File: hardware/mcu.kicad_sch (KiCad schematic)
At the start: 36 parts, among them U1 74LVC125, U2 STM32F407VETx, U3 24LC64, U7 74LVC125, X1 12MHz

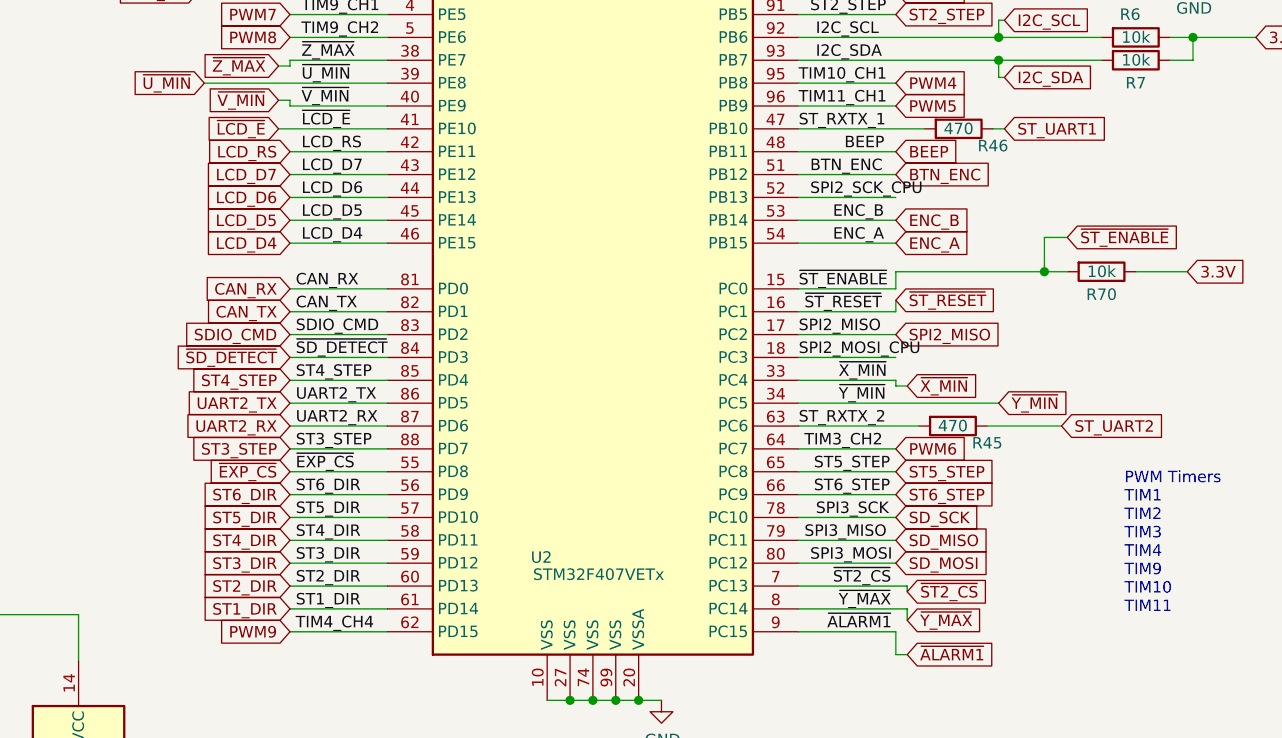
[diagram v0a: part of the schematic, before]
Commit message: Wire sd-card to SPI1, add sd_card_ss (~SD_CS) pin. Add EXP_CD pin for EXP2.4. Add dedicated EXP_SS pin for EXP2.7 - no longer has to share ~SD_DETECT. Added new pin ~EXP_CS2, replaced 3.3V supply on EXP3.
Removed 3.3V power supply from extension header. The 3.3V power supply is
very limited (500mA) and we need it clean for the ADCs to work well.
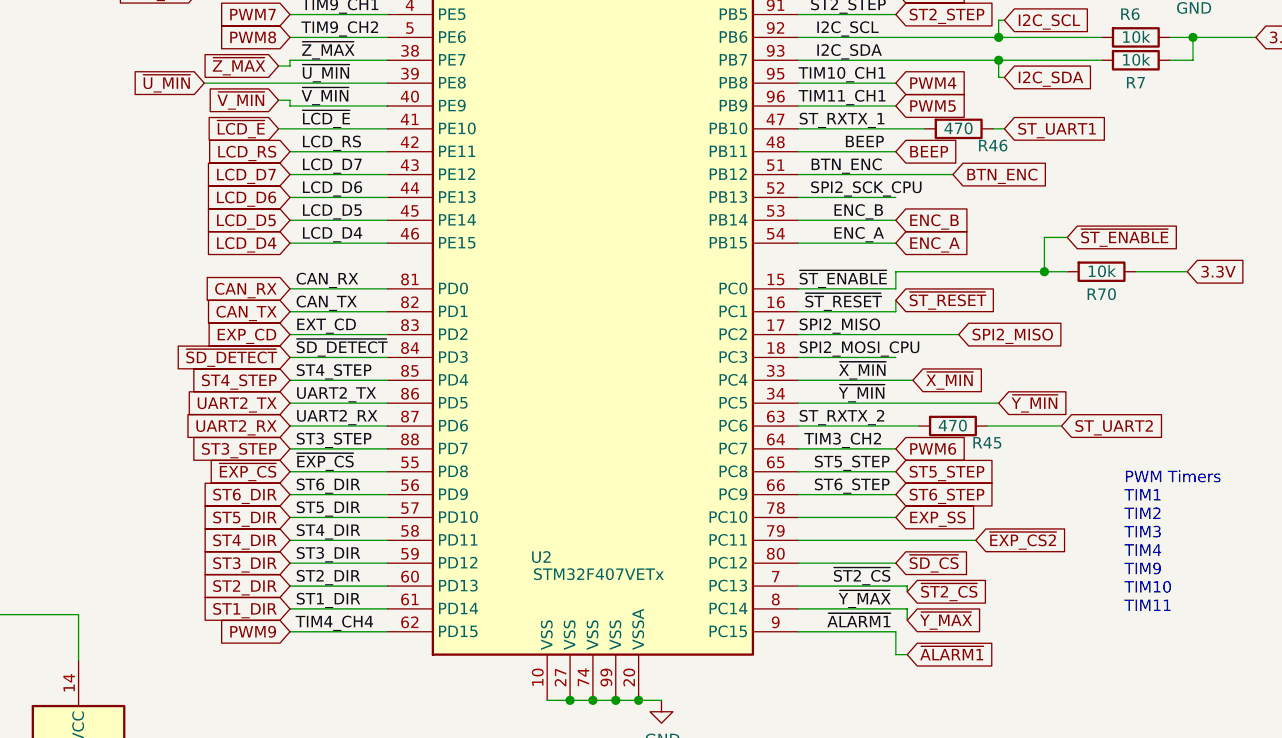
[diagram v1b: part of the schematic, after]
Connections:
- net SDIO_CMD renamed EXP_CD
- net SD_MISO renamed ~EXP_CS2
- net SD_MOSI renamed ~SD_CS
- net SD_SCK renamed EXP_SS
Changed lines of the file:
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@@
     (stroke (width 0) (type solid) (color 0 0 0 0))
   )
-  (wire (pts (xy 126.365 105.41) (xy 137.16 105.41))
+  (wire (pts (xy 126.365 105.41) (xy 143.51 105.41))
     (stroke (width 0) (type solid) (color 0 0 0 0))
   )
@@
     (stroke (width 0) (type solid) (color 0 0 0 0))
   )
-  (wire (pts (xy 126.365 123.19) (xy 137.16 123.19))
+  (wire (pts (xy 126.365 123.19) (xy 144.145 123.19))
     (stroke (width 0) (type solid) (color 0 0 0 0))
   )
@@
     (stroke (width 0) (type solid) (color 0 0 0 0))
   )
-  (wire (pts (xy 126.365 128.27) (xy 137.16 128.27))
+  (wire (pts (xy 126.365 128.27) (xy 139.065 128.27))
     (stroke (width 0) (type solid) (color 0 0 0 0))
   )
@@
     (stroke (width 0) (type solid) (color 0 0 0 0))
   )
-  (wire (pts (xy 126.365 146.05) (xy 137.16 146.05))
+  (wire (pts (xy 126.365 146.05) (xy 146.05 146.05))
     (stroke (width 0) (type solid) (color 0 0 0 0))
   )
@@
     (stroke (width 0) (type solid) (color 0 0 0 0))
   )
-  (wire (pts (xy 137.16 128.905) (xy 137.16 128.27))
-    (stroke (width 0) (type solid) (color 0 0 0 0))
-  )
   (wire (pts (xy 137.16 158.75) (xy 137.16 156.21))
     (stroke (width 0) (type solid) (color 0 0 0 0))
   )
-  (wire (pts (xy 138.43 128.905) (xy 137.16 128.905))
-    (stroke (width 0) (type solid) (color 0 0 0 0))
-  )
   (wire (pts (xy 138.43 151.13) (xy 138.43 151.765))
     (stroke (width 0) (type solid) (color 0 0 0 0))
@@
     (effects (font (size 1.27 1.27)) (justify left bottom))
   )
-  (label "SDIO_CMD" (at 70.485 123.19 0)
+  (label "EXT_CD" (at 70.485 123.19 0)
     (effects (font (size 1.27 1.27)) (justify left bottom))
   )
@@
     (effects (font (size 1.27 1.27)) (justify left bottom))
   )
-  (label "SPI3_MISO" (at 127 146.05 0)
-    (effects (font (size 1.27 1.27)) (justify left bottom))
-  )
   (label "SPI2_MOSI_CPU" (at 127 174.625 0)
     (effects (font (size 1.27 1.27)) (justify left bottom))
@@
     (effects (font (size 1.27 1.27)) (justify left bottom))
   )
-  (label "SPI3_MOSI" (at 127.635 148.59 0)
-    (effects (font (size 1.27 1.27)) (justify left bottom))
-  )
   (label "UART_TX" (at 128.27 54.61 0)
     (effects (font (size 1.27 1.27)) (justify left bottom))
@@
   )
   (label "I2C_SDA" (at 128.27 92.71 0)
-    (effects (font (size 1.27 1.27)) (justify left bottom))
-  )
-  (label "SPI3_SCK" (at 128.27 143.51 0)
     (effects (font (size 1.27 1.27)) (justify left bottom))
   )
@@
     (effects (font (size 1.27 1.27)) (justify right))
   )
-  (global_label "SDIO_CMD" (shape input) (at 69.85 123.19 180)    (property "Intersheet References" "${INTERSHEET_REFS}" (id 0) (at 0 0 0)
-      (effects (font (size 1.27 1.27)) hide)
+  (global_label "EXP_CD" (shape input) (at 69.85 123.19 180)    (property "Intersheet References" "${INTERSHEET_REFS}" (id 0) (at 58.7767 123.1106 0)
+      (effects (font (size 1.27 1.27)) (justify right) hide)
     )
     (effects (font (size 1.27 1.27)) (justify right))
@@
     (effects (font (size 1.27 1.27)) (justify left))
   )
-  (global_label "BTN_ENC" (shape input) (at 137.16 105.41 0)    (property "Intersheet References" "${INTERSHEET_REFS}" (id 0) (at 0 0 0)
-      (effects (font (size 1.27 1.27)) hide)
-    )
-    (effects (font (size 1.27 1.27)) (justify left))
-  )
   (global_label "ENC_B" (shape input) (at 137.16 110.49 0)    (property "Intersheet References" "${INTERSHEET_REFS}" (id 0) (at 0 0 0)
       (effects (font (size 1.27 1.27)) hide)
@@
     (effects (font (size 1.27 1.27)) (justify left))
   )
-  (global_label "SPI2_MISO" (shape input) (at 137.16 123.19 0)    (property "Intersheet References" "${INTERSHEET_REFS}" (id 0) (at 0 0 0)
-      (effects (font (size 1.27 1.27)) hide)
-    )
-    (effects (font (size 1.27 1.27)) (justify left))
-  )
   (global_label "PWM6" (shape input) (at 137.16 135.89 0)    (property "Intersheet References" "${INTERSHEET_REFS}" (id 0) (at 0 0 0)
       (effects (font (size 1.27 1.27)) hide)
@@
     (effects (font (size 1.27 1.27)) (justify left))
   )
-  (global_label "SD_SCK" (shape input) (at 137.16 143.51 0)    (property "Intersheet References" "${INTERSHEET_REFS}" (id 0) (at 148.2938 143.4306 0)
+  (global_label "EXP_SS" (shape input) (at 137.16 143.51 0)    (property "Intersheet References" "${INTERSHEET_REFS}" (id 0) (at 148.1123 143.4306 0)
       (effects (font (size 1.27 1.27)) (justify left) hide)
     )
     (effects (font (size 1.27 1.27)) (justify left))
   )
-  (global_label "SD_MISO" (shape input) (at 137.16 146.05 0)    (property "Intersheet References" "${INTERSHEET_REFS}" (id 0) (at 149.1404 145.9706 0)
+  (global_label "~SD_CS" (shape input) (at 137.16 148.59 0)    (property "Intersheet References" "${INTERSHEET_REFS}" (id 0) (at 147.0238 148.5106 0)
       (effects (font (size 1.27 1.27)) (justify left) hide)
     )
     (effects (font (size 1.27 1.27)) (justify left))
   )
-  (global_label "SD_MOSI" (shape input) (at 137.16 148.59 0)    (property "Intersheet References" "${INTERSHEET_REFS}" (id 0) (at 149.1404 148.5106 0)
+  (global_label "~ST2_CS" (shape input) (at 138.43 151.765 0)    (property "Intersheet References" "${INTERSHEET_REFS}" (id 0) (at 0 0 0)
+      (effects (font (size 1.27 1.27)) hide)
+    )
+    (effects (font (size 1.27 1.27)) (justify left))
+  )
+  (global_label "~Y_MAX" (shape input) (at 138.43 154.94 0)    (property "Intersheet References" "${INTERSHEET_REFS}" (id 0) (at 0 0 0)
+      (effects (font (size 1.27 1.27)) hide)
+    )
+    (effects (font (size 1.27 1.27)) (justify left))
+  )
+  (global_label "~ALARM1" (shape input) (at 138.43 158.75 0)    (property "Intersheet References" "${INTERSHEET_REFS}" (id 0) (at 0 0 0)
+      (effects (font (size 1.27 1.27)) hide)
+    )
+    (effects (font (size 1.27 1.27)) (justify left))
+  )
+  (global_label "~X_MIN" (shape input) (at 139.065 128.27 0)    (property "Intersheet References" "${INTERSHEET_REFS}" (id 0) (at 0.635 -0.635 0)
+      (effects (font (size 1.27 1.27)) hide)
+    )
+    (effects (font (size 1.27 1.27)) (justify left))
+  )
+  (global_label "BTN_ENC" (shape input) (at 143.51 105.41 0)    (property "Intersheet References" "${INTERSHEET_REFS}" (id 0) (at 6.35 0 0)
+      (effects (font (size 1.27 1.27)) hide)
+    )
+    (effects (font (size 1.27 1.27)) (justify left))
+  )
+  (global_label "SPI2_MISO" (shape input) (at 144.145 123.19 0)    (property "Intersheet References" "${INTERSHEET_REFS}" (id 0) (at 6.985 0 0)
+      (effects (font (size 1.27 1.27)) hide)
+    )
+    (effects (font (size 1.27 1.27)) (justify left))
+  )
+  (global_label "~EXP_CS2" (shape input) (at 146.05 146.05 0)    (property "Intersheet References" "${INTERSHEET_REFS}" (id 0) (at 158.2723 145.9706 0)
       (effects (font (size 1.27 1.27)) (justify left) hide)
     )
     (effects (font (size 1.27 1.27)) (justify left))
-  )
-  (global_label "~X_MIN" (shape input) (at 138.43 128.905 0)    (property "Intersheet References" "${INTERSHEET_REFS}" (id 0) (at 0 0 0)
-      (effects (font (size 1.27 1.27)) hide)
-    )
-    (effects (font (size 1.27 1.27)) (justify left))
-  )
-  (global_label "~ST2_CS" (shape input) (at 138.43 151.765 0)    (property "Intersheet References" "${INTERSHEET_REFS}" (id 0) (at 0 0 0)
-      (effects (font (size 1.27 1.27)) hide)
-    )
-    (effects (font (size 1.27 1.27)) (justify left))
-  )
-  (global_label "~Y_MAX" (shape input) (at 138.43 154.94 0)    (property "Intersheet References" "${INTERSHEET_REFS}" (id 0) (at 0 0 0)
-      (effects (font (size 1.27 1.27)) hide)
-    )
-    (effects (font (size 1.27 1.27)) (justify left))
-  )
-  (global_label "~ALARM1" (shape input) (at 138.43 158.75 0)    (property "Intersheet References" "${INTERSHEET_REFS}" (id 0) (at 0 0 0)
-      (effects (font (size 1.27 1.27)) hide)
-    )
-    (effects (font (size 1.27 1.27)) (justify left))

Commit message: Convert SCH files to latest version. Fix DRC Warnings in PrntrBoard.
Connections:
- net ~ALARM1 renamed ~{ALARM1}
- net ~EXP_CS renamed ~{EXP_CS}
- net ~EXP_CS2 renamed ~{EXP_CS2}
- net ~LCD_E renamed ~{LCD_E}
- net ~RESET renamed ~{RESET}
- net ~SD_CS renamed ~{SD_CS}
- net ~SD_DETECT renamed ~{SD_DETECT}
- net ~ST1_CS renamed ~{ST1_CS}
- net ~ST2_CS renamed ~{ST2_CS}
- net ~ST3_CS renamed ~{ST3_CS}
- net ~ST4_CS renamed ~{ST4_CS}
- net ~ST5_CS renamed ~{ST5_CS}
- net ~ST6_CS renamed ~{ST6_CS}
- net ~ST_ENABLE renamed ~{ST_ENABLE}
- net ~ST_RESET renamed ~{ST_RESET}
- net ~U_MIN renamed ~{U_MIN}
- net ~V_MIN renamed ~{V_MIN}
- net ~X_MAX renamed ~{X_MAX}
- net ~X_MIN renamed ~{X_MIN}
- net ~Y_MAX renamed ~{Y_MAX}
- net ~Y_MIN renamed ~{Y_MIN}
- net ~Z_MAX renamed ~{Z_MAX}
- net ~Z_MIN renamed ~{Z_MIN}

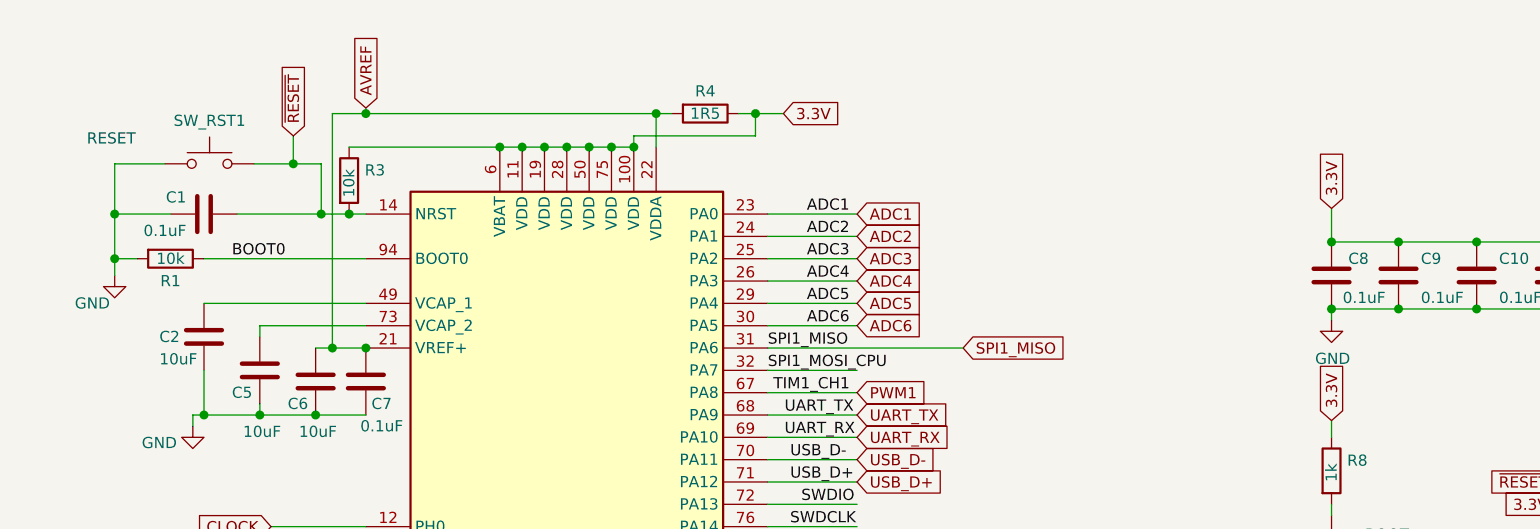
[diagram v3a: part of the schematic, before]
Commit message: Improve ADC ground: add separate GNDA bus; add ferrite bead to AVREF power.
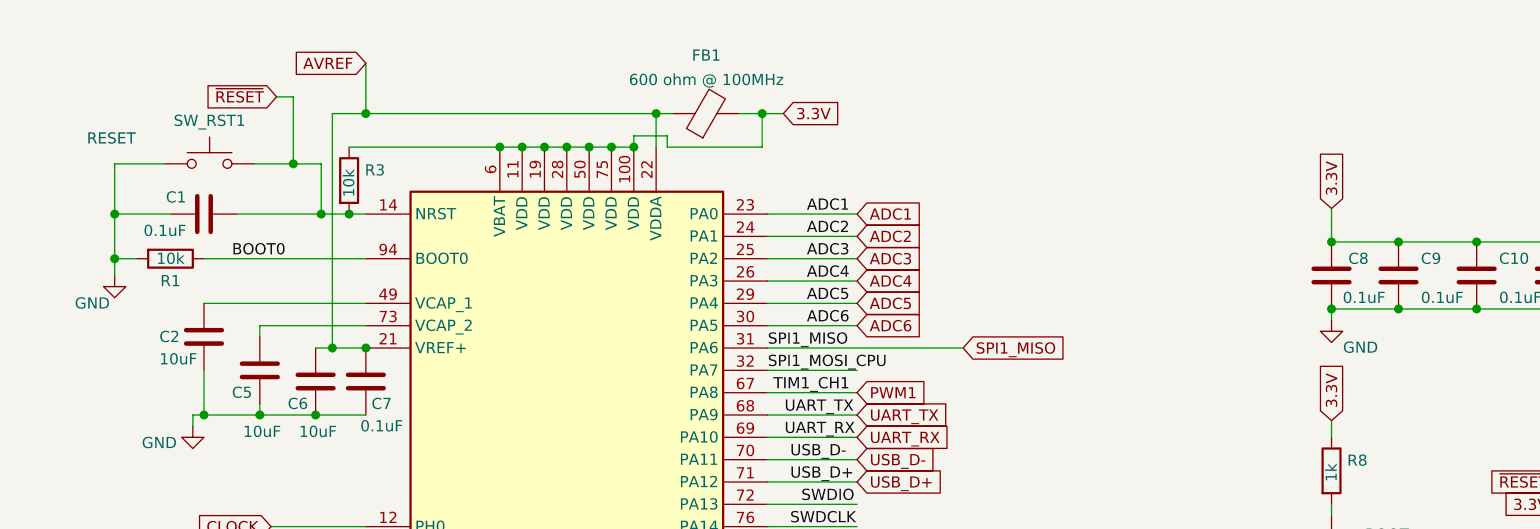
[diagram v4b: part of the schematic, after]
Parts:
- removed R4: 1R5, PrntrBoardV2:R_0603_1608Metric, symbol Device:R
- added FB1: 600 ohm @ 100MHz, Inductor_SMD:L_0805_2012Metric, symbol Device:Ferrite_Bead
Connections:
- net 3.3V: now also FB1.2
- net AVREF: now also FB1.1
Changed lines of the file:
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@@
   (junction (at 111.125 24.13) (diameter 1.016) (color 0 0 0 0))
   (junction (at 113.665 20.32) (diameter 1.016) (color 0 0 0 0))
-  (junction (at 124.968 20.32) (diameter 1.016) (color 0 0 0 0))
+  (junction (at 125.73 20.32) (diameter 1.016) (color 0 0 0 0))
   (junction (at 146.05 80.01) (diameter 1.016) (color 0 0 0 0))
   (junction (at 148.59 90.17) (diameter 1.016) (color 0 0 0 0))
@@
     (stroke (width 0) (type solid) (color 0 0 0 0))
   )
+  (wire (pts (xy 70.485 18.415) (xy 72.39 18.415))
+    (stroke (width 0) (type solid) (color 0 0 0 0))
+  )
   (wire (pts (xy 70.485 177.8) (xy 86.995 177.8))
     (stroke (width 0) (type solid) (color 0 0 0 0))
   )
-  (wire (pts (xy 72.39 22.86) (xy 72.39 26.035))
+  (wire (pts (xy 72.39 18.415) (xy 72.39 26.035))
     (stroke (width 0) (type solid) (color 0 0 0 0))
   )
@@
     (stroke (width 0) (type solid) (color 0 0 0 0))
   )
-  (wire (pts (xy 80.645 19.685) (xy 80.645 20.32))
+  (wire (pts (xy 80.645 14.605) (xy 80.645 20.32))
     (stroke (width 0) (type solid) (color 0 0 0 0))
   )
@@
     (stroke (width 0) (type solid) (color 0 0 0 0))
   )
-  (wire (pts (xy 111.125 22.86) (xy 124.968 22.86))
-    (stroke (width 0) (type solid) (color 0 0 0 0))
-  )
-  (wire (pts (xy 111.125 24.13) (xy 111.125 22.86))
+  (wire (pts (xy 111.125 22.86) (xy 111.125 24.13))
     (stroke (width 0) (type solid) (color 0 0 0 0))
   )
@@
     (stroke (width 0) (type solid) (color 0 0 0 0))
   )
-  (wire (pts (xy 113.665 20.32) (xy 115.443 20.32))
-    (stroke (width 0) (type solid) (color 0 0 0 0))
-  )
-  (wire (pts (xy 123.063 20.32) (xy 124.968 20.32))
-    (stroke (width 0) (type solid) (color 0 0 0 0))
-  )
-  (wire (pts (xy 124.968 20.32) (xy 128.143 20.32))
-    (stroke (width 0) (type solid) (color 0 0 0 0))
-  )
-  (wire (pts (xy 124.968 22.86) (xy 124.968 20.32))
+  (wire (pts (xy 113.665 20.32) (xy 115.57 20.32))
+    (stroke (width 0) (type solid) (color 0 0 0 0))
+  )
+  (wire (pts (xy 114.935 22.86) (xy 111.125 22.86))
+    (stroke (width 0) (type solid) (color 0 0 0 0))
+  )
+  (wire (pts (xy 114.935 24.13) (xy 114.935 22.86))
+    (stroke (width 0) (type solid) (color 0 0 0 0))
+  )
+  (wire (pts (xy 123.19 20.32) (xy 125.73 20.32))
+    (stroke (width 0) (type solid) (color 0 0 0 0))
+  )
+  (wire (pts (xy 125.73 20.32) (xy 128.143 20.32))
+    (stroke (width 0) (type solid) (color 0 0 0 0))
+  )
+  (wire (pts (xy 125.73 24.13) (xy 114.935 24.13))
+    (stroke (width 0) (type solid) (color 0 0 0 0))
+  )
+  (wire (pts (xy 125.73 24.13) (xy 125.73 20.32))
     (stroke (width 0) (type solid) (color 0 0 0 0))
   )
@@
     )
   )
-  (global_label "~{RESET}" (shape input) (at 72.39 22.86 90)
-    (effects (font (size 1.27 1.27)) (justify left))
-    (property "Intersheet References" "${INTERSHEET_REFS}" (id 0) (at 0 0 0)
-      (effects (font (size 1.27 1.27)) hide)
-    )
-  )
-  (global_label "AVREF" (shape input) (at 80.645 19.685 90)
-    (effects (font (size 1.27 1.27)) (justify left))
-    (property "Intersheet References" "${INTERSHEET_REFS}" (id 0) (at 0 0 0)
+  (global_label "~{RESET}" (shape input) (at 70.485 18.415 180)
+    (effects (font (size 1.27 1.27)) (justify right))
+    (property "Intersheet References" "${INTERSHEET_REFS}" (id 0) (at 47.625 90.805 0)
+      (effects (font (size 1.27 1.27)) hide)
+    )
+  )
+  (global_label "AVREF" (shape input) (at 80.645 14.605 180)
+    (effects (font (size 1.27 1.27)) (justify right))
+    (property "Intersheet References" "${INTERSHEET_REFS}" (id 0) (at 60.96 95.25 0)
       (effects (font (size 1.27 1.27)) hide)
     )
@@
       (effects (font (size 1.27 1.27)) hide)
     )
-    (property "Value" "GND" (id 1) (at 190.627 48.2092 0))
+    (property "Value" "GND" (id 1) (at 193.802 46.9392 0))
     (property "Footprint" "" (id 2) (at 190.5 43.815 0)
       (effects (font (size 1.27 1.27)) hide)
@@
     (pin "2")
   )
-  (symbol (lib_id "Device:R") (at 119.253 20.32 270) (unit 1)
-    (in_bom yes) (on_board yes)
-    (property "Reference" "R4" (id 0) (at 119.253 17.78 90))
-    (property "Value" "1R5" (id 1) (at 119.253 20.32 90))
-    (property "Footprint" "PrntrBoardV2:R_0603_1608Metric" (id 2) (at 119.253 18.542 90)
-      (effects (font (size 1.27 1.27)) hide)
-    )
-    (property "Datasheet" "~" (id 3) (at 119.253 20.32 0)
-      (effects (font (size 1.27 1.27)) hide)
-    )
-    (property "Part #" "0603WAF220KT5E" (id 4) (at 119.253 20.32 0)
-      (effects (font (size 1.27 1.27)) hide)
-    )
-    (property "LCSC Part #" "C22939" (id 5) (at 119.253 20.32 0)
-      (effects (font (size 1.27 1.27)) hide)
-    )
-    (pin "1")
-    (pin "2")
-  )
   (symbol (lib_id "Device:R") (at 143.51 133.35 270) (unit 1)
     (in_bom yes) (on_board yes)
@@
       (effects (font (size 1.27 1.27)) hide)
     )
+    (pin "1")
+    (pin "2")
+  )
+  (symbol (lib_id "Device:Ferrite_Bead") (at 119.38 20.32 90) (unit 1)
+    (in_bom yes) (on_board yes) (fields_autoplaced)
+    (property "Reference" "FB1" (id 0) (at 119.38 13.7118 90))
+    (property "Value" "600 ohm @ 100MHz" (id 1) (at 119.38 16.4869 90))
+    (property "Footprint" "Inductor_SMD:L_0805_2012Metric" (id 2) (at 119.38 22.098 90)
+      (effects (font (size 1.27 1.27)) hide)
+    )
+    (property "Datasheet" "~" (id 3) (at 119.38 20.32 0)
+      (effects (font (size 1.27 1.27)) hide)
+    )
+    (property "Part #" "GZ2012D601TF" (id 4) (at 119.38 20.32 90)
+      (effects (font (size 1.27 1.27)) hide)
+    )
+    (property "LCSC Part #" "C1017" (id 5) (at 119.38 20.32 90)
+      (effects (font (size 1.27 1.27)) hide)
+    )
